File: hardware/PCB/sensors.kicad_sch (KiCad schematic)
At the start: 20 parts, among them IC2 IIS2MDCTR, J1 IMU_EXT, J2 GPS, J9 Conn_01x05_Socket, U6 LSM6DSOXTR, U7 BME280, U8 INA219BxDCN, U9 INA219BxDCN

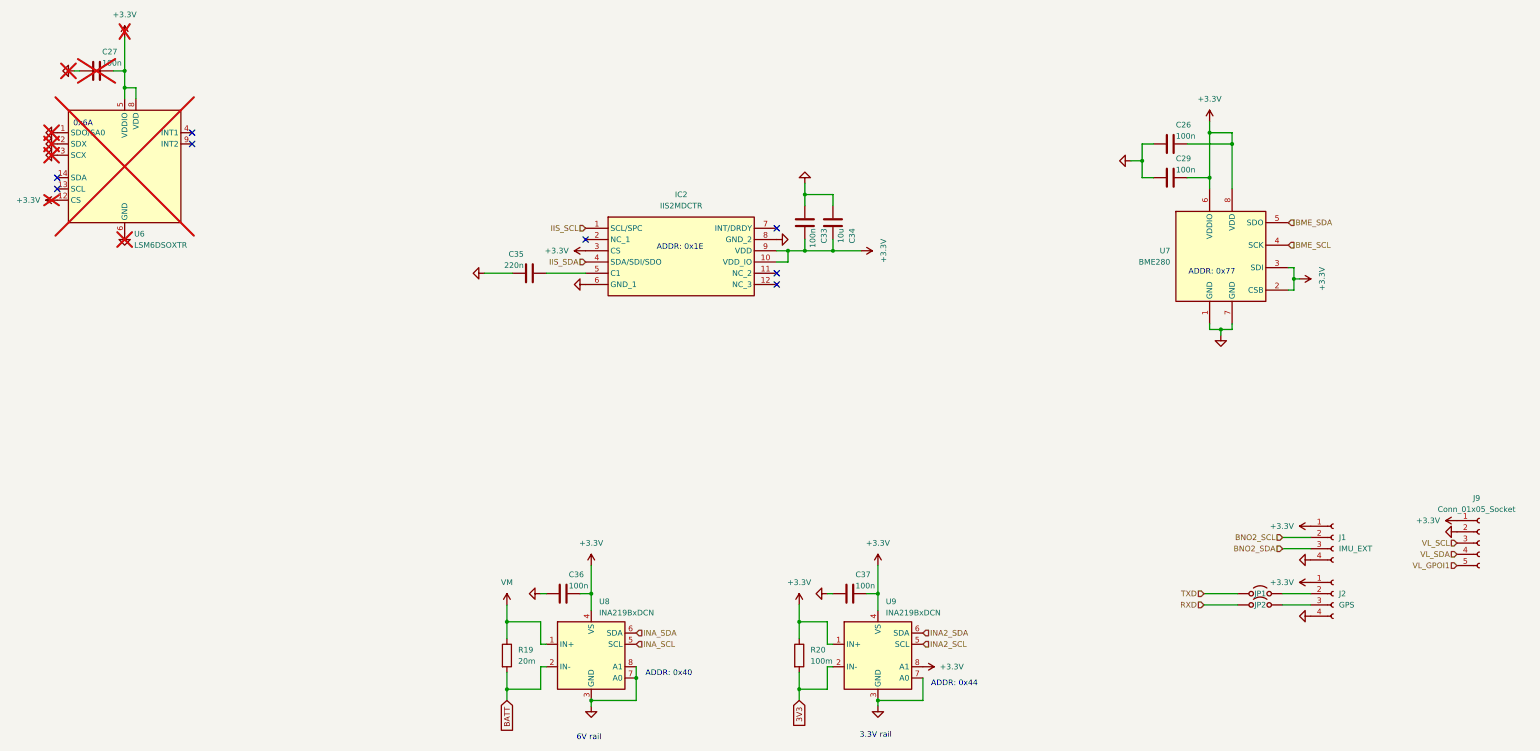
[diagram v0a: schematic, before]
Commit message: Added external QMC5883L instead of on-PCB IIS2MDCTR
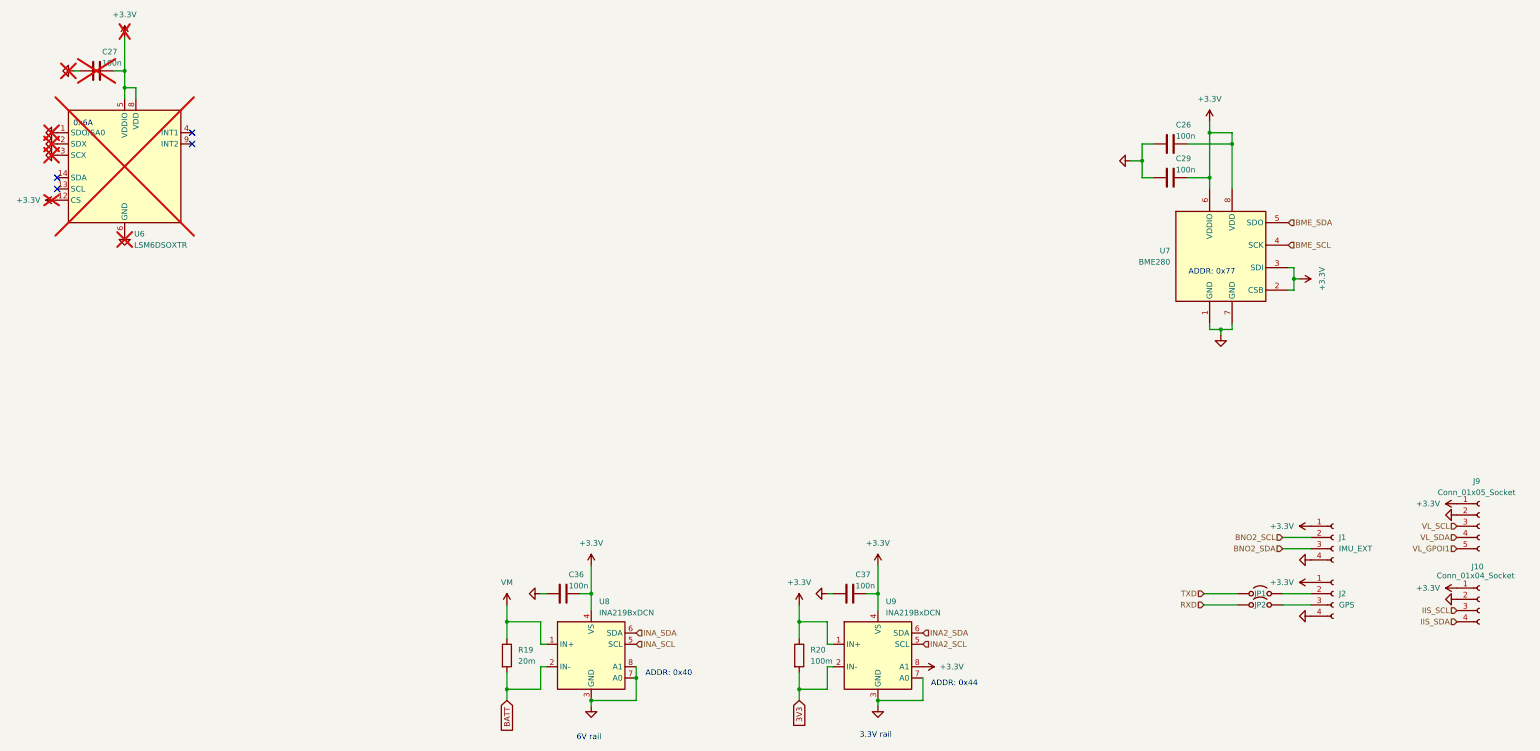
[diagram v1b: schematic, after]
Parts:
- removed C33: 100n, Capacitor_SMD:C_1206_3216Metric_Pad1.33x1.80mm_HandSolder, symbol Device:C
- removed C34: 10u, Capacitor_SMD:C_1210_3225Metric_Pad1.33x2.70mm_HandSolder, symbol Device:C
- removed C35: 220n, Capacitor_SMD:C_1206_3216Metric_Pad1.33x1.80mm_HandSolder, symbol Device:C
- removed IC2: IIS2MDCTR, Package_LGA:LGA-12_2x2mm_P0.5mm, symbol IIS2MDCTR:IIS2MDCTR
- added J10: Conn_01x04_Socket, Connector_PinSocket_2.54mm:PinSocket_1x04_P2.54mm_Vertical, symbol Connector:Conn_01x04_Socket
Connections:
- net +3.3V: now also J10.1 (Pin_1)
- net GND: now also J10.2 (Pin_2)
- net IIS_SCL: now also J10.3 (Pin_3)
- net IIS_SDA: now also J10.4 (Pin_4)
- no-connect marks 8 -> 4
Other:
- note removed: "ADDR: 0x1E"
- moved on the sheet: J9

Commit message: Removed polar azimuth motor driver from pcb
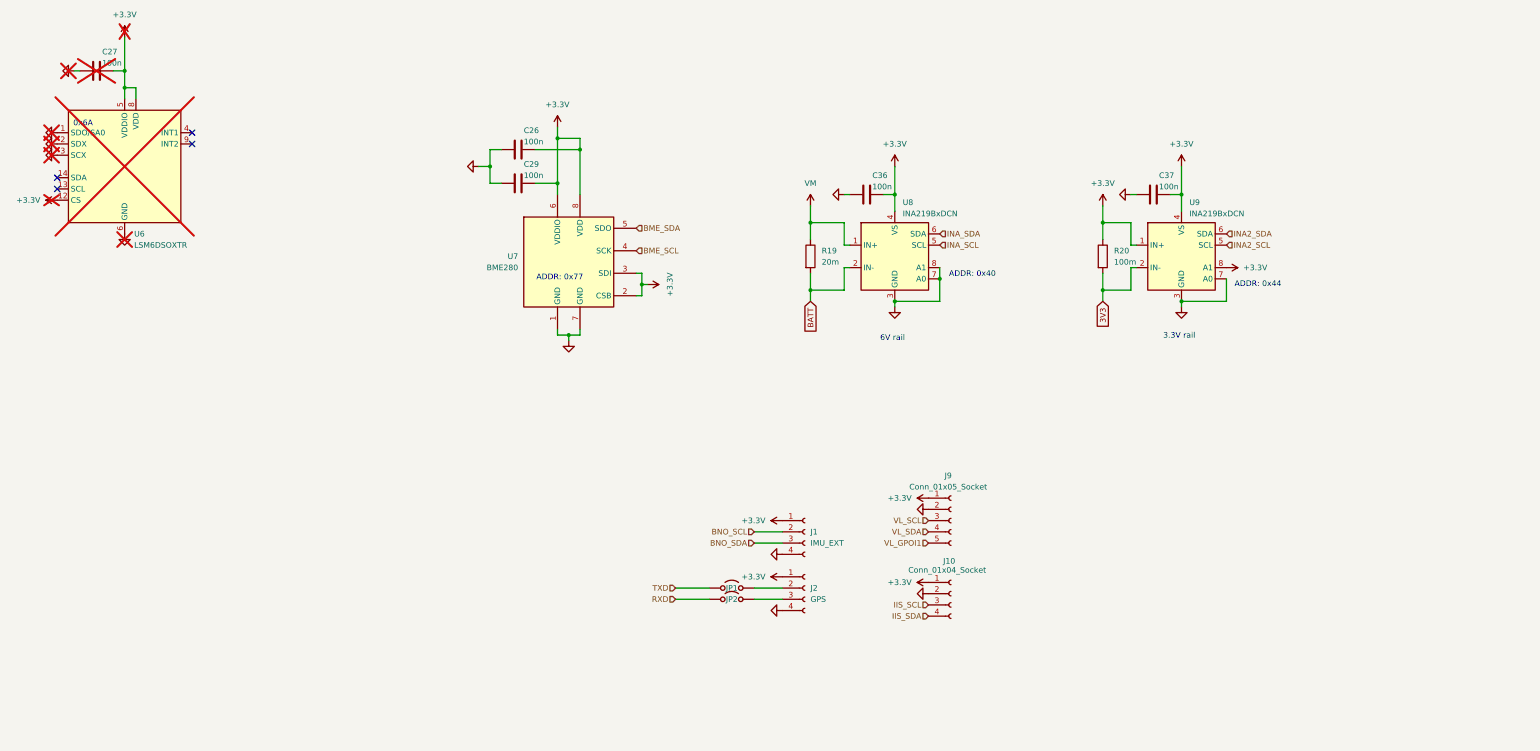
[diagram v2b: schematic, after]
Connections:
- net BNO2_SCL renamed BNO_SCL
- net BNO2_SDA renamed BNO_SDA
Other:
- moved on the sheet: C26, C29, C36, C37, J1, J10, J2, J9, JP1, JP2, R19, R20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
